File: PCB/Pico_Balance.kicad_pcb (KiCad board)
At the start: 2 copper layers, 100 x 52 mm, 42 parts, among them J1 XT60PW-M, J2 GPIO_Ext, J3 Conn_Motor0, J4 Conn_Motor1, J5 5V3A OUT, Q1 CSD17577Q3A, U1 BMI160, U2 DRV8876PWPR, U3 DRV8876PWPR, U4 LM74610QDGKRQ1, U5 LMR51430

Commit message: Small refinements
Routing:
- net GND: track 10.0 -> 13.5 mm
- net OUT1: track 17.5 -> 18.6 mm
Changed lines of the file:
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@@
 			(unlocked yes)
 			(layer "F.SilkS")
+			(hide yes)
 			(effects
 				(font
@@
 			(at 0 -2.5 0)
 			(layer "F.SilkS")
+			(hide yes)
 			(effects
 				(font
@@
 			(at 0 -1.43 90)
 			(layer "F.SilkS")
+			(hide yes)
 			(effects
 				(font
@@
 			(at 0 -1.43 90)
 			(layer "F.SilkS")
+			(hide yes)
 			(effects
 				(font
@@
 			(at 0 -1.43 0)
 			(layer "F.SilkS")
+			(hide yes)
 			(effects
 				(font
@@
 			(at -0.127 -1.905 90)
 			(layer "F.SilkS")
+			(hide yes)
 			(effects
 				(font
@@
 			(at 1.27 -2.38 180)
 			(layer "F.SilkS")
+			(hide yes)
 			(effects
 				(font
@@
 			(at 0 -1.43 0)
 			(layer "F.SilkS")
+			(hide yes)
 			(effects
 				(font
@@
 	)
 	(segment
+		(start 158.575 94.075)
+		(end 158.85 94.35)
+		(width 0.45)
+		(layer "F.Cu")
+		(net 8)
+	)
+	(segment
 		(start 192.6 83.85)
 		(end 193.35 84.6)
@@
 	)
 	(segment
+		(start 161.825003 90.825001)
+		(end 161.55 90.549998)
+		(width 0.45)
+		(layer "F.Cu")
+		(net 8)
+	)
+	(segment
 		(start 245.6625 88.7675)
 		(end 245.6625 87.5625)
@@
 	)
 	(segment
+		(start 157.250001 94.075)
+		(end 158.575 94.075)
+		(width 0.45)
+		(layer "F.Cu")
+		(net 8)
+	)
+	(segment
 		(start 246.65 89.48)
 		(end 246.65 89.13)
@@
 	)
 	(segment
+		(start 163.150002 90.825001)
+		(end 161.825003 90.825001)
+		(width 0.45)
+		(layer "F.Cu")
+		(net 8)
+	)
+	(segment
 		(start 191.4125 81.05)
 		(end 192.074999 81.05)
@@
 		(net 57)
 	)
+	(segment
+		(start 156.274999 94.725001)
+		(end 156.2 94.8)
+		(width 0.45)
+		(layer "F.Cu")
+		(net 58)
+	)
+	(segment
+		(start 157.250001 94.725001)
+		(end 156.274999 94.725001)
+		(width 0.45)
+		(layer "F.Cu")
+		(net 58)
+	)
 	(via

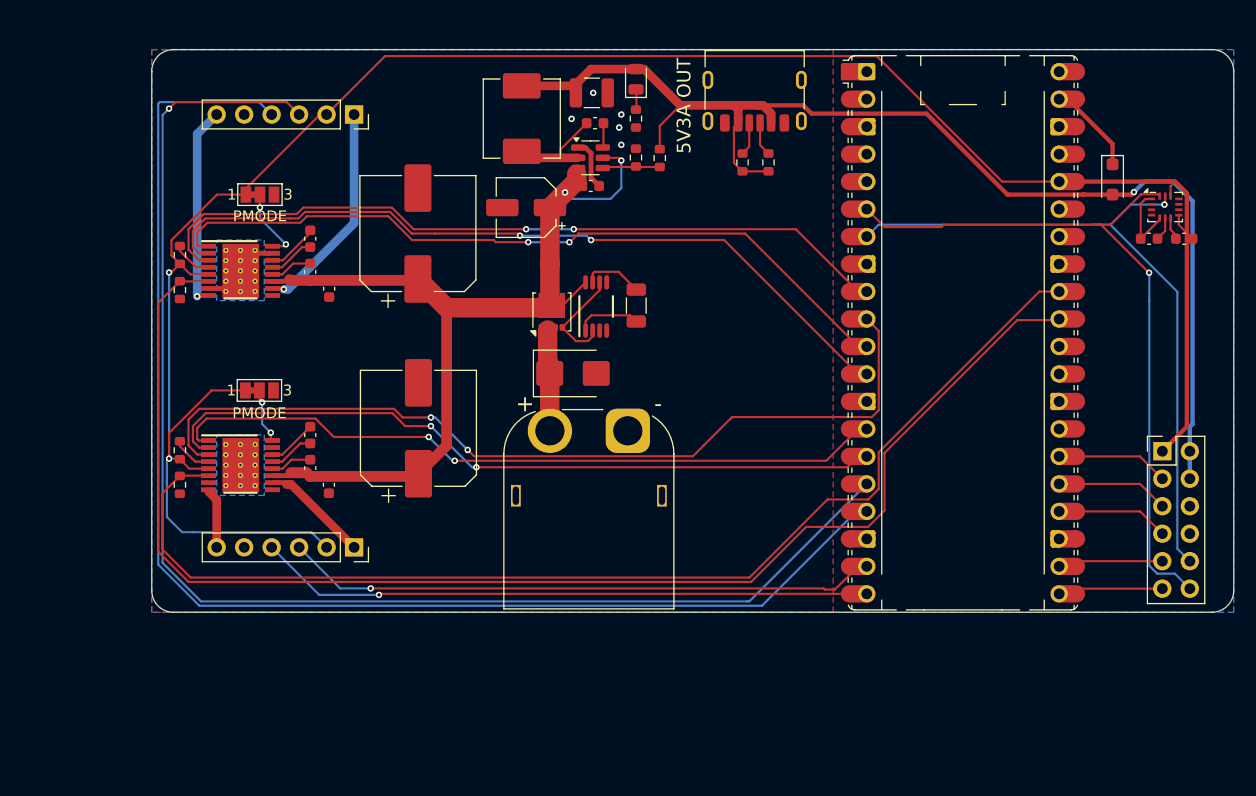
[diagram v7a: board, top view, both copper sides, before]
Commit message: Silkscreen and minor layout changes
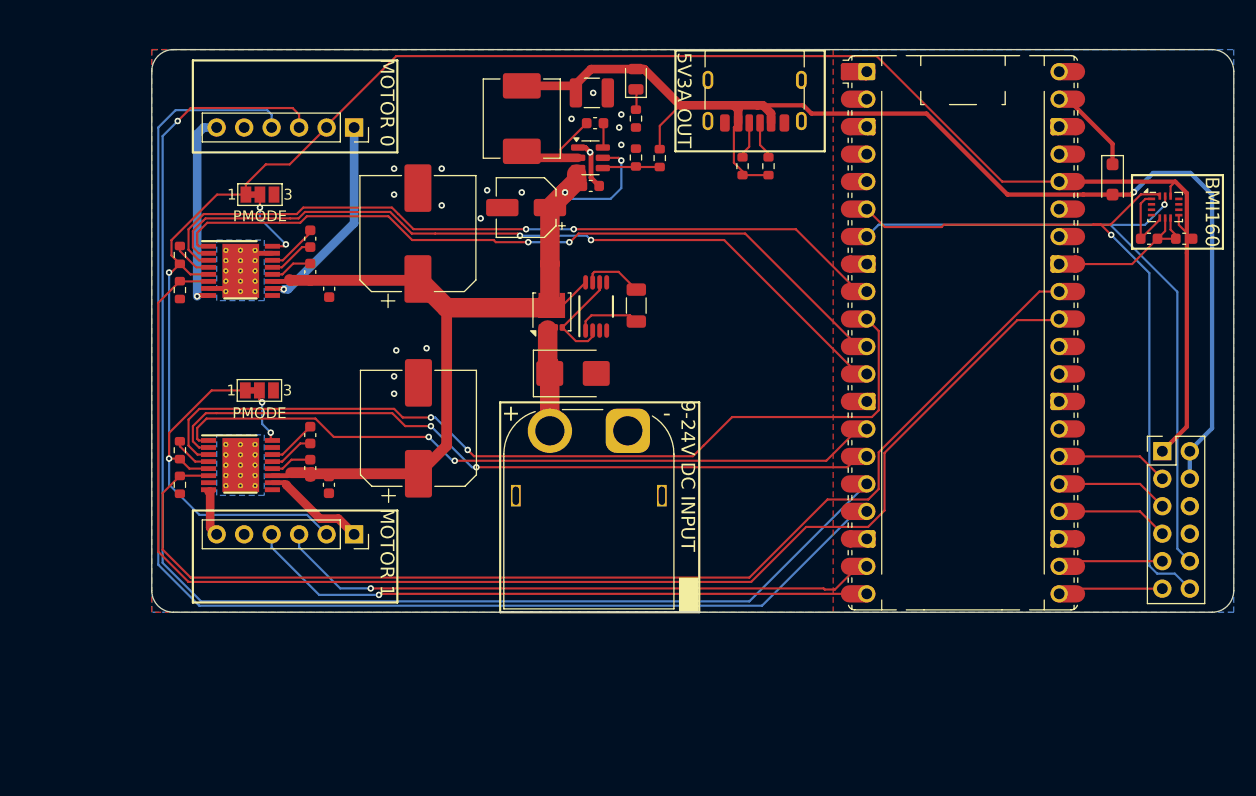
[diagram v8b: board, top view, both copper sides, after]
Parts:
- moved J3 1.20 mm to (170.7, 79.2)
- moved J4 1.20 mm to (170.7, 116.8)
- moved R8 0.35 mm to (209.0, 82.8)
- moved R9 0.35 mm to (206.6, 82.8)
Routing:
- net GND: track 13.5 -> 24.4 mm, vias 5 -> 17
- net +5V: track 112.2 -> 116.1 mm
- net +3V3: track 203.1 -> 200.9 mm
- net OUT2: track 20.2 -> 19.0 mm
- net ENCB1: track 56.1 -> 57.3 mm
- net ENCA1: track 54.2 -> 55.4 mm
- net OUT3: track 5.46 -> 4.35 mm
- net VM: track 86.6 -> 85.5 mm
- net OUT4: track 10.5 -> 9.56 mm
- net ENCB0: track 124.3 -> 123.6 mm
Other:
- board text added: "9-24V DC INPUT"
- board text added: "MOTOR 0"
- board text added: "MOTOR 1"
